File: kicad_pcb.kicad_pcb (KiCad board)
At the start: 2 copper layers, 285 x 99.4 mm, 164 parts, among them J1 USB_B_Mini, SW1 SW_Push, U1 ATmega32U4-AU, Y1 16Mhz

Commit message: Added Katana60 logo to gerbers
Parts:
- added G***: LOGO, bitmaps:katana60_logo, B.Cu at (206.4, 96.8)

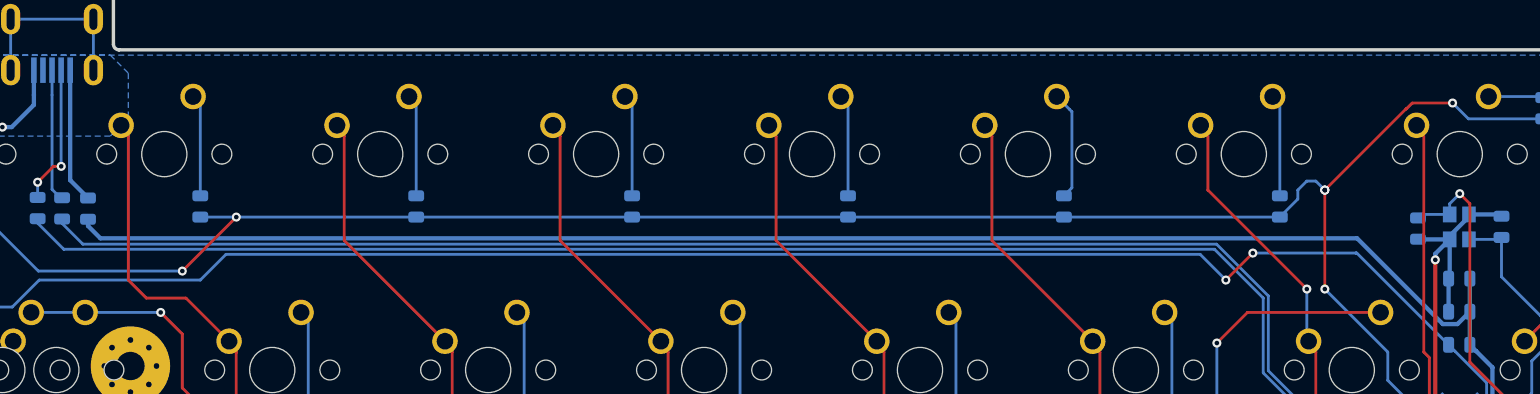
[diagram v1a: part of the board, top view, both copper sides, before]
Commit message: ammended some incorrect footprints
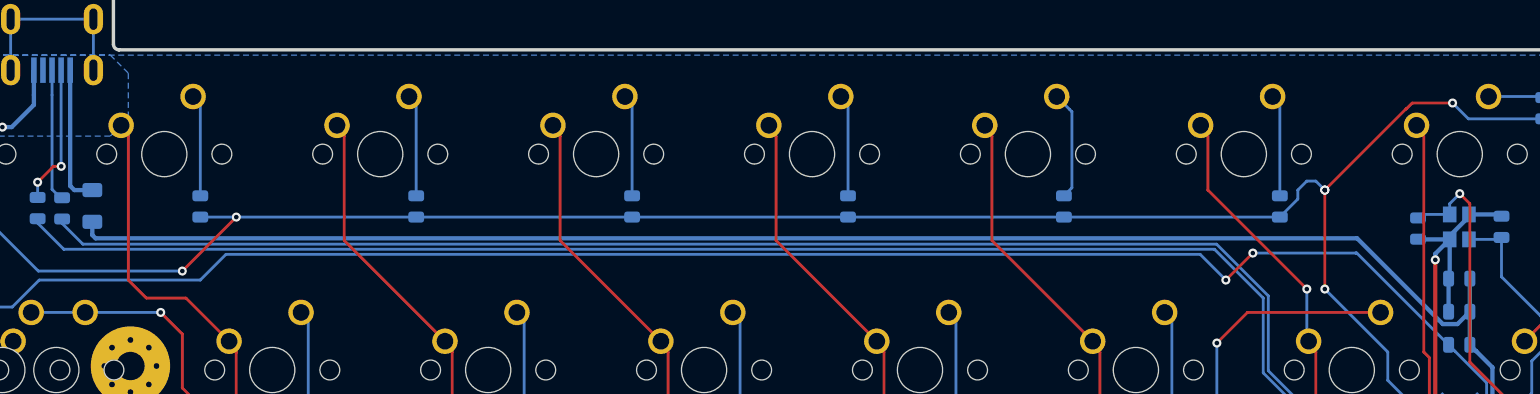
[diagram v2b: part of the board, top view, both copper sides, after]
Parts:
- C7: value 0.1uF -> 10uF
- F1: footprint Fuse:Fuse_0805_2012Metric -> Fuse:Fuse_1206_3216Metric
- moved F1 0.45 mm to (85.7, 53.8)

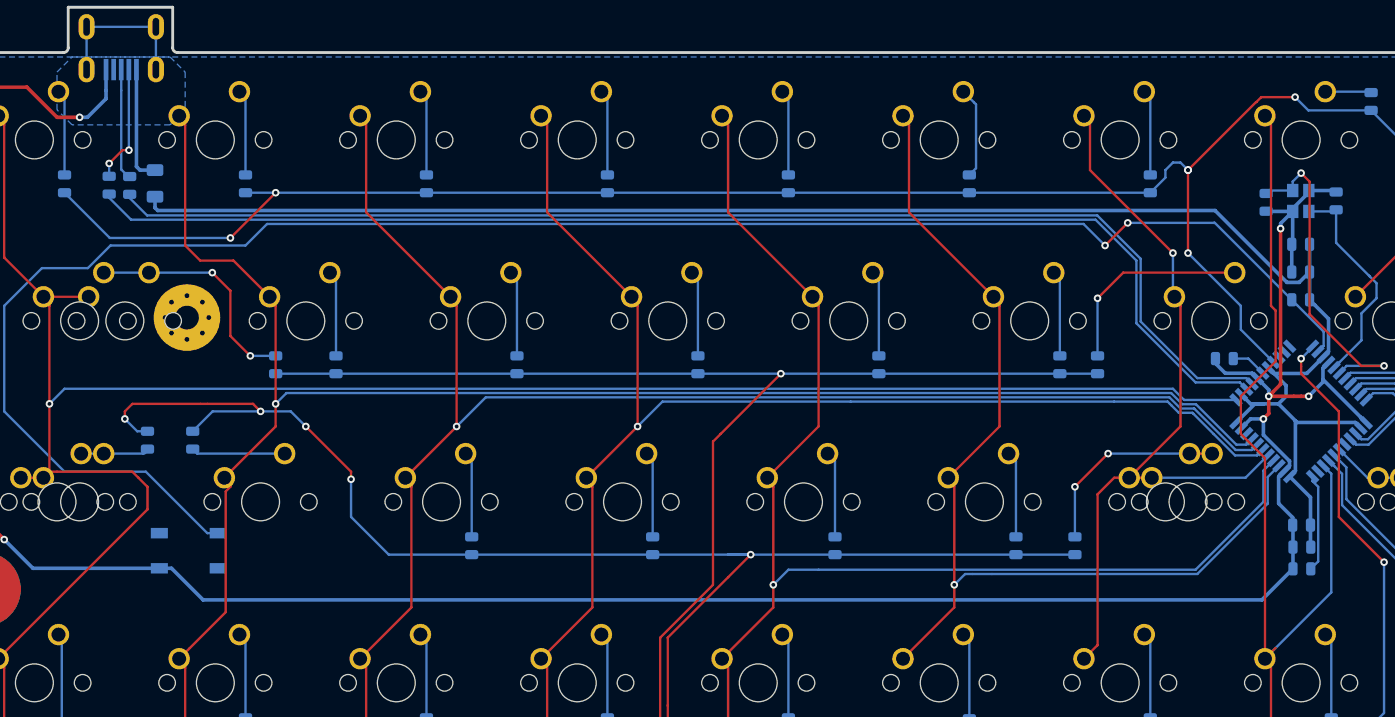
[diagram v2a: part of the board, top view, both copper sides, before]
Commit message: Moved and re-routed traces for C7 decoupling capacitor
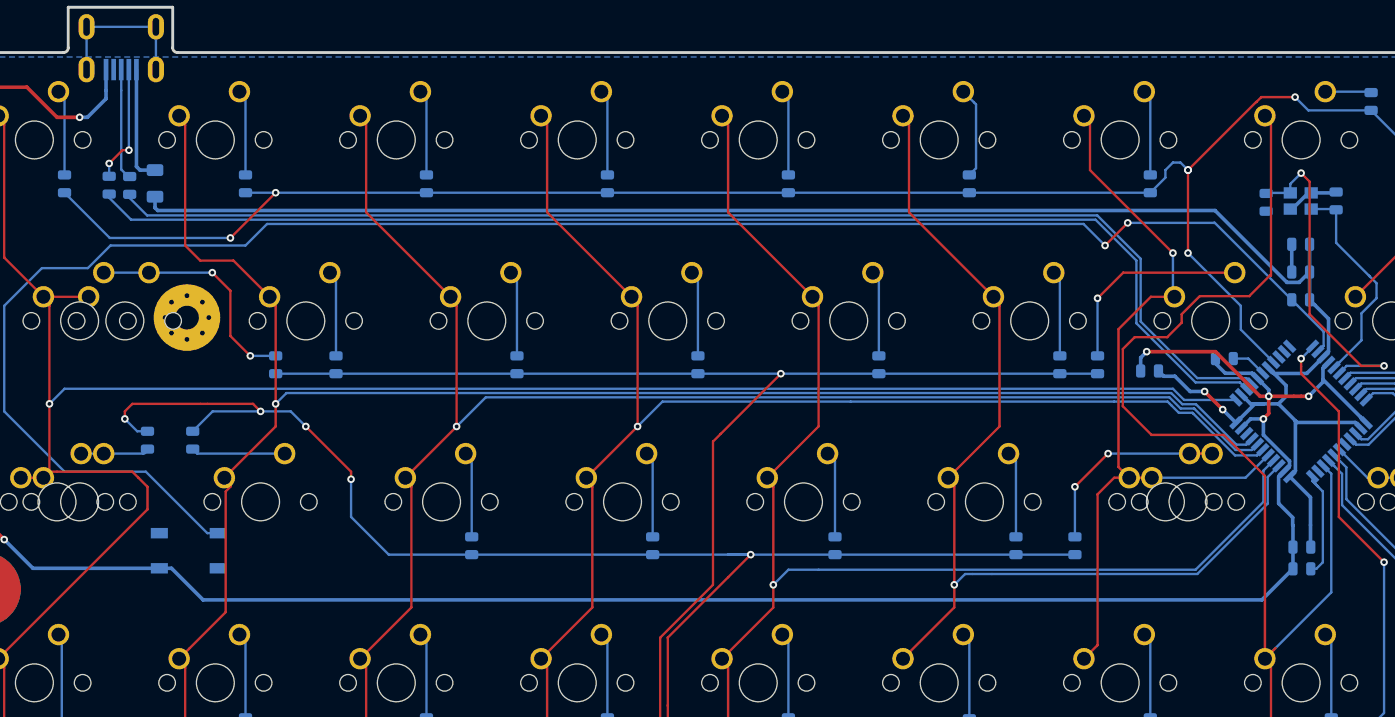
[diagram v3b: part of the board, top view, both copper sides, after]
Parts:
- moved C7 22.8 mm to (190.4, 73.5)
- turned Y1 to 0 degrees
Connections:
- Y1 pad 1: GND -> Net-(C1-Pad1)
- Y1 pad 2: Net-(C2-Pad1) -> GND
- Y1 pad 3: GND -> Net-(C2-Pad1)
- Y1 pad 4: Net-(C1-Pad1) -> GND
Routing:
- net COL7: track 104.9 -> 124.4 mm
- net +5V: track 183.2 -> 193.7 mm, vias 0 -> 2
- net GND: track 289.7 -> 280.6 mm
- net COL6: track 82.1 -> 84.0 mm
- net Net-(R4-Pad2): track 10.3 -> 11.6 mm

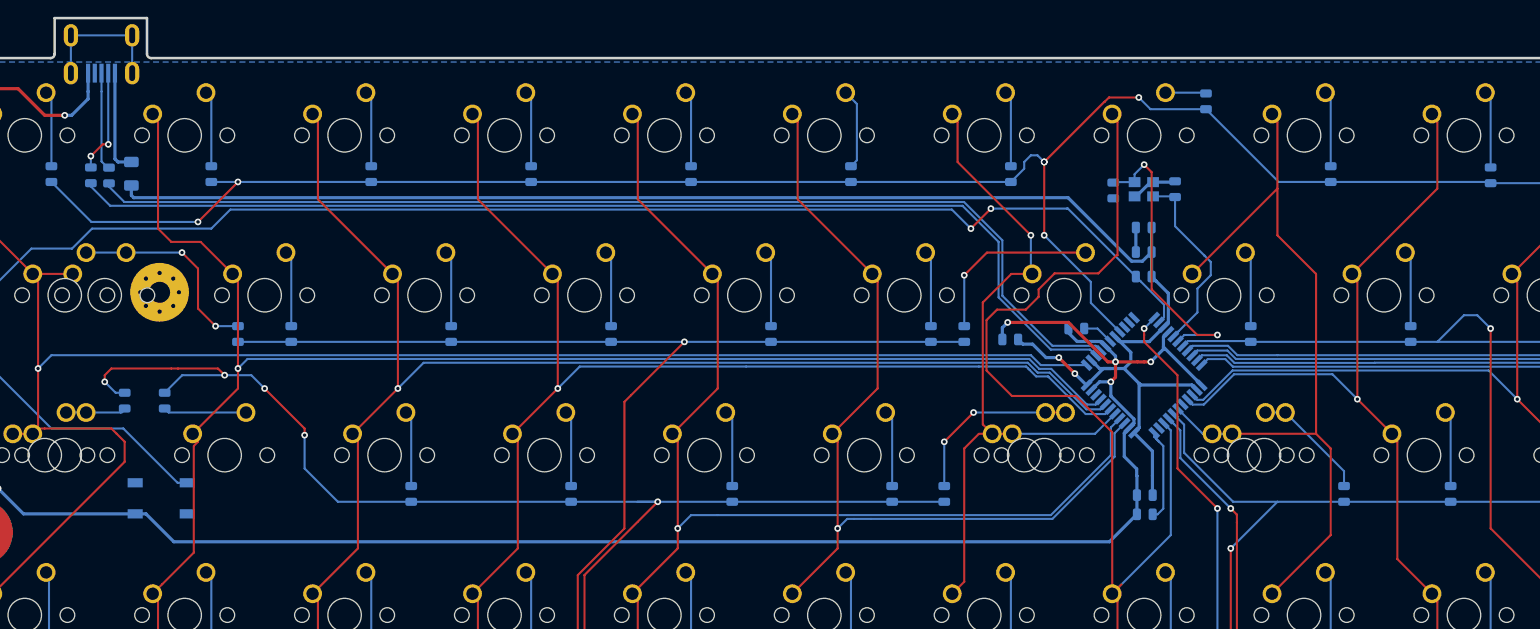
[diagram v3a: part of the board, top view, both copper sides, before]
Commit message: started to restructure the routing
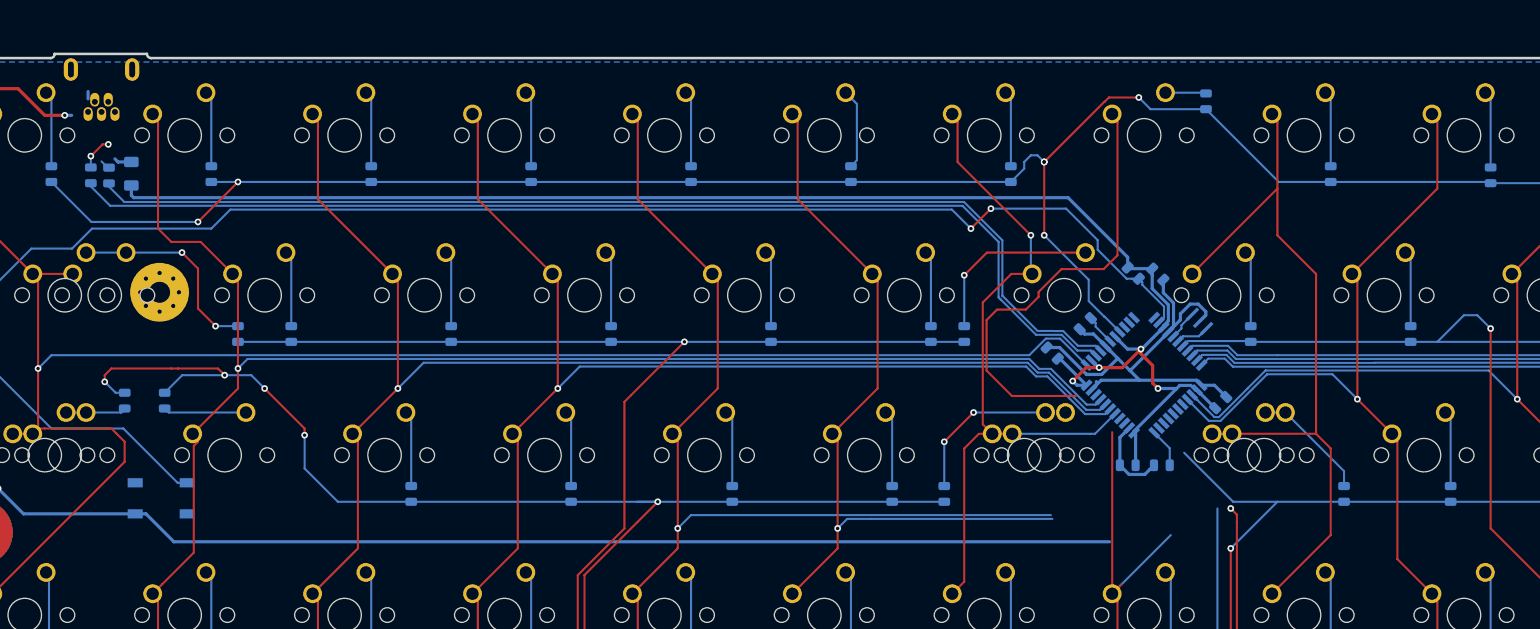
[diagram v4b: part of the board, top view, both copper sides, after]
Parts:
- removed C1, C2: 22pF, Capacitor_SMD:C_0805_2012Metric
- J1: footprint random-keyboard-parts:Molex-0548190589 -> random-keyboard-parts:Molex-0548190519
- Y1: value 16Mhz -> Resonator_Small; footprint Crystal:Crystal_SMD_3225-4Pin_3.2x2.5mm -> Crystal:Resonator_SMD_muRata_CSTxExxV-3Pin_3.0x1.1mm
- moved C4 20.1 mm to (215.5, 81.1), turned to 45 degrees
- moved Y1 17.1 mm to (213.0, 71.4), turned to 135 degrees
- moved R4 6.19 mm to (208.5, 88.5)
- moved C6 5.81 mm to (208.0, 65.8), turned to 315 degrees
- moved C7 5.26 mm to (195.4, 75.2), turned to 135 degrees
- moved C5 4.10 mm to (204.4, 88.5)
- moved J1 2.32 mm to (82.2, 39.6)
- moved R1 1.31 mm to (205.1, 65.6), turned to 135 degrees
- moved C3 1.21 mm to (199.4, 71.7), turned to 225 degrees
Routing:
- net Net-(U1-Pad17): track 35.9 -> 4.06 mm, vias 2 -> 0
- net ROW3: track 311.3 -> 284.4 mm, vias 2 -> 0
- net Net-(U1-Pad16): track 24.1 -> 3.61 mm
- net COL7: track 124.4 -> 104.4 mm
- net Net-(J1-Pad6): track 16.3 -> 0.00 mm
- net COL5: track 107.1 -> 92.2 mm
- net COL4: track 164.6 -> 149.7 mm
- net ROW4: track 319.5 -> 305.8 mm
- net GND: track 280.6 -> 268.7 mm, vias 6 -> 2
- net D+: track 11.8 -> 1.26 mm
- net VCC: track 12.3 -> 2.11 mm
- net +5V: track 193.7 -> 185.1 mm, vias 2 -> 4
- net D-: track 12.6 -> 4.17 mm
- net Net-(R4-Pad2): track 11.6 -> 4.64 mm
- net COL8: track 95.0 -> 89.7 mm
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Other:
- board size 285 x 99.4 mm -> 285 x 95.1 mm

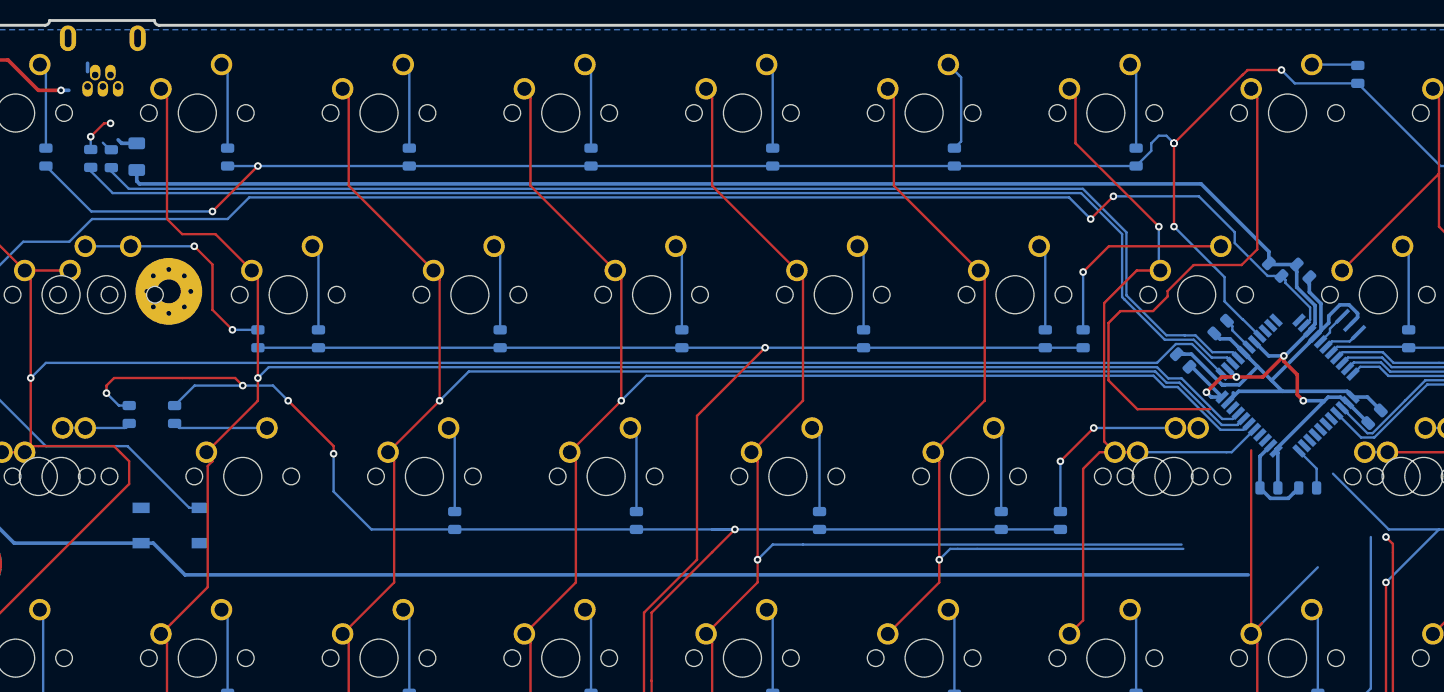
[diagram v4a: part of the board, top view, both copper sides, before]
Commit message: finished tracing repositioned componenets
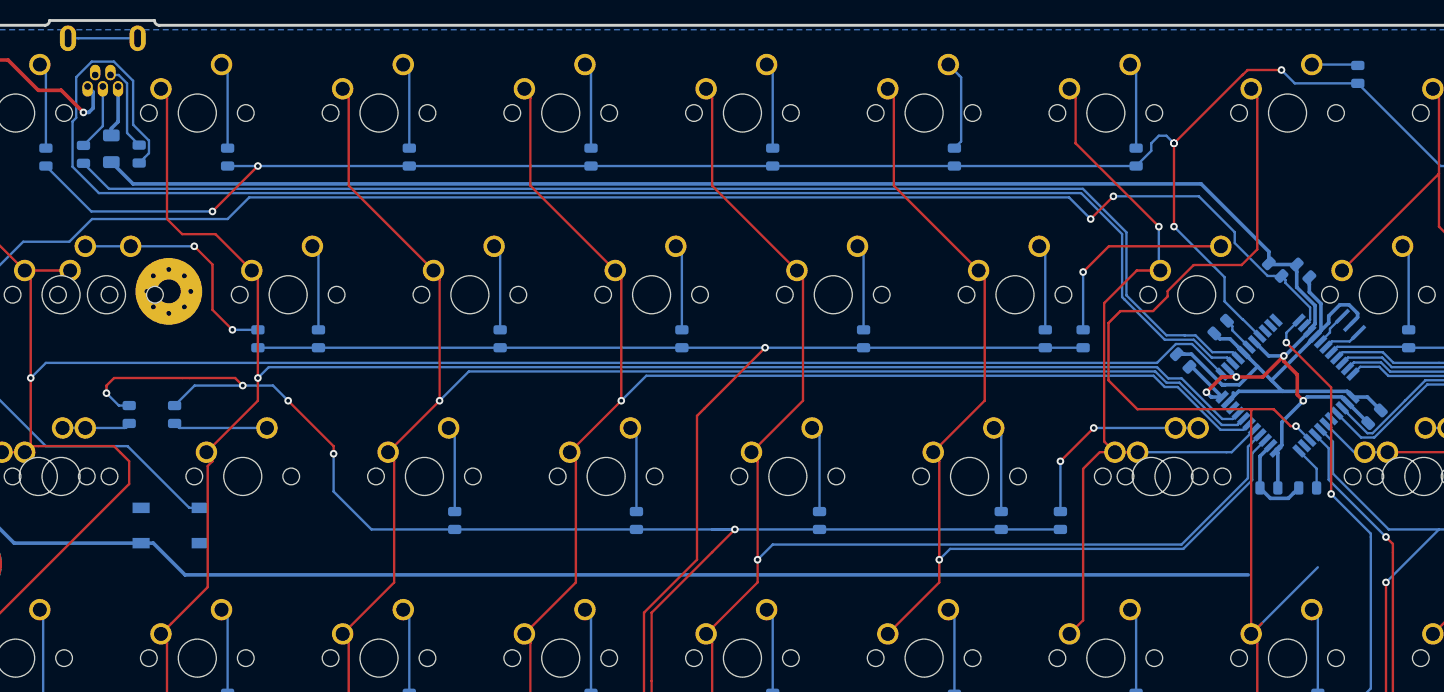
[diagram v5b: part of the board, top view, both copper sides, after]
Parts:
- moved R3 5.10 mm to (86.0, 53.5)
- moved R2 2.96 mm to (80.1, 53.5)
- moved F1 2.79 mm to (83.1, 53.0)
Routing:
- net Net-(R3-Pad1): track 132.5 -> 160.8 mm
- net ROW3: track 284.4 -> 311.4 mm, vias 0 -> 2
- net COL7: track 104.4 -> 120.6 mm, vias 0 -> 1
- net COL5: track 92.2 -> 107.1 mm
- net COL4: track 149.7 -> 164.6 mm
- net ROW4: track 305.8 -> 319.5 mm
- net Net-(J1-Pad6): track 0.00 -> 7.30 mm
- net D+: track 1.26 -> 7.03 mm
- net GND: track 268.7 -> 274.1 mm
- net COL8: track 89.7 -> 95.0 mm
- net ROW2: track 359.7 -> 364.9 mm
- net D-: track 4.17 -> 9.11 mm, vias 2 -> 0
- net VCC: track 2.11 -> 5.43 mm
- net Net-(R2-Pad1): track 130.7 -> 133.4 mm
- net Net-(D37-Pad2): track 18.8 -> 21.2 mm
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
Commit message: improved capacitor traces again
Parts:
- moved R1 130.4 mm to (74.8, 59.0), turned to 0 degrees
- moved C6 3.17 mm to (206.2, 63.1), turned to 0 degrees
- moved C4 2.98 mm to (217.4, 78.8), turned to 90 degrees
- moved C7 0.45 mm to (195.7, 74.8), turned to 315 degrees
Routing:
- net +5V: track 186.8 -> 287.3 mm, vias 4 -> 9
- net Net-(R1-Pad1): track 191.2 -> 199.6 mm
- net GND: track 274.1 -> 281.4 mm, vias 2 -> 5
- net COL7: track 120.6 -> 116.3 mm
- net ROW3: track 311.4 -> 313.7 mm
- net COL10: track 128.7 -> 126.9 mm
- net COL9: track 113.9 -> 112.3 mm
- net Net-(R3-Pad1): track 160.8 -> 162.3 mm, vias 0 -> 2
- net COL0: track 230.6 -> 229.2 mm, vias 1 -> 3
- net Net-(R2-Pad1): track 133.4 -> 134.8 mm, vias 0 -> 2
- net COL11: track 144.1 -> 143.5 mm
- net COL5: track 107.1 -> 107.4 mm, vias 1 -> 3
- net COL4: track 164.6 -> 164.4 mm, vias 1 -> 3
- net Net-(D37-Pad2): vias 2 -> 1

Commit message: made more improvements to the routing
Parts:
- moved C3 0.64 mm to (199.9, 71.3)
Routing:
- net +5V: track 287.3 -> 298.4 mm, vias 9 -> 7
- net GND: track 281.4 -> 271.4 mm, vias 5 -> 4
- net ROW4: track 319.5 -> 322.6 mm
- net ROW0: track 299.6 -> 301.0 mm
- net ROW1: track 444.0 -> 442.7 mm
- net Net-(R3-Pad1): vias 2 -> 4
- net Net-(R2-Pad1): vias 2 -> 4

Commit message: further routing
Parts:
- moved R1 26.9 mm to (88.9, 81.9), turned to 90 degrees
- moved D45 15.4 mm to (338.5, 91.9)
- moved D32 15.2 mm to (100.0, 91.9), turned to 90 degrees
- moved D37 15.1 mm to (197.6, 91.9)
- moved D16 12.7 mm to (85.7, 72.9)
- moved D31 11.8 mm to (81.0, 91.9), turned to 90 degrees
- moved D8 9.89 mm to (209.6, 54.1)
- moved R4 7.61 mm to (200.9, 89.6), turned to 45 degrees
- moved C5 7.60 mm to (211.9, 89.7), turned to 315 degrees
- moved C3 7.46 mm to (205.1, 66.0), turned to 270 degrees
- moved Y1 7.01 mm to (216.7, 77.3), turned to 90 degrees
- moved D39 6.36 mm to (223.8, 92.2)
- moved C4 5.63 mm to (215.8, 73.4), turned to 180 degrees
- moved C6 3.17 mm to (207.6, 66.0), turned to 270 degrees
- moved C7 3.13 mm to (193.8, 72.4)
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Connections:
- U1 pad 1: COL0 -> ROW1
- U1 pad 12: ROW3 -> Net-(U1-Pad12)
- U1 pad 18: ROW1 -> COL14
- U1 pad 19: COL14 -> COL13
- U1 pad 20: COL13 -> COL12
- U1 pad 21: COL12 -> COL11
- U1 pad 22: COL11 -> ROW2
- U1 pad 25: COL10 -> ROW3
- U1 pad 26: COL9 -> ROW4
- U1 pad 28: COL8 -> COL10
- U1 pad 29: ROW2 -> COL9
- U1 pad 30: ROW4 -> COL8
- U1 pad 32: Net-(U1-Pad32) -> COL6
- U1 pad 38: COL6 -> COL3
- U1 pad 39: COL3 -> COL2
- U1 pad 40: COL2 -> COL1
- U1 pad 41: COL1 -> COL0
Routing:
- net ROW4: track 322.6 -> 0.00 mm, vias 2 -> 0
- net GND: track 271.4 -> 38.8 mm, vias 4 -> 0
- net Net-(R1-Pad1): track 199.6 -> 11.6 mm, vias 2 -> 0
- net ROW1: track 442.7 -> 285.2 mm, vias 4 -> 2
- net COL7: track 116.3 -> 0.00 mm, vias 1 -> 0
- net ROW2: track 364.9 -> 261.8 mm, vias 8 -> 0
- net COL10: track 126.9 -> 65.5 mm, vias 1 -> 0
- net COL4: track 164.4 -> 112.3 mm, vias 3 -> 1
- net ROW3: track 313.7 -> 266.7 mm, vias 2 -> 0
- net COL9: track 112.3 -> 65.5 mm, vias 1 -> 0
- net Net-(R3-Pad1): track 162.3 -> 131.2 mm, vias 4 -> 2
- net COL14: track 246.0 -> 223.3 mm, vias 1 -> 0
- net COL8: track 95.0 -> 78.2 mm, vias 0 -> 1
- net COL13: track 183.6 -> 168.0 mm, vias 1 -> 0
- net ROW0: track 301.0 -> 316.6 mm, vias 6 -> 0
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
